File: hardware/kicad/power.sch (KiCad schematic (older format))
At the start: 12 parts, among them U2 ME6210, U3 ME6210, U4 TLV61046ADB

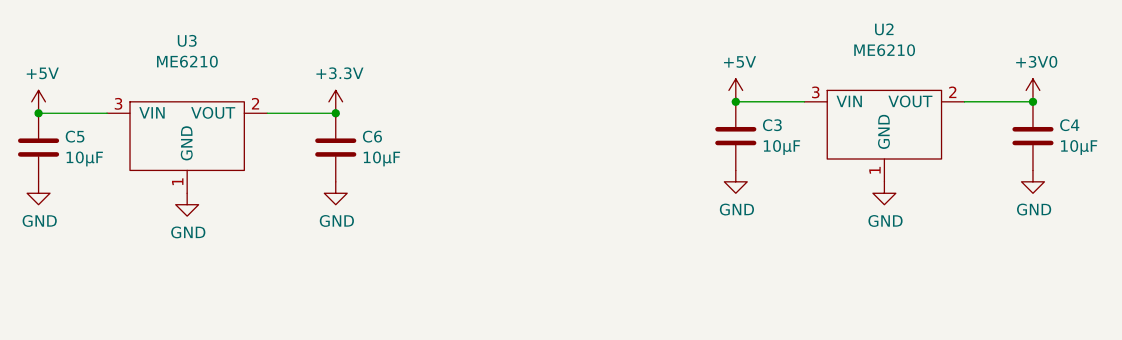
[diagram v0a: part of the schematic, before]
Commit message: Carify power IC symbol names
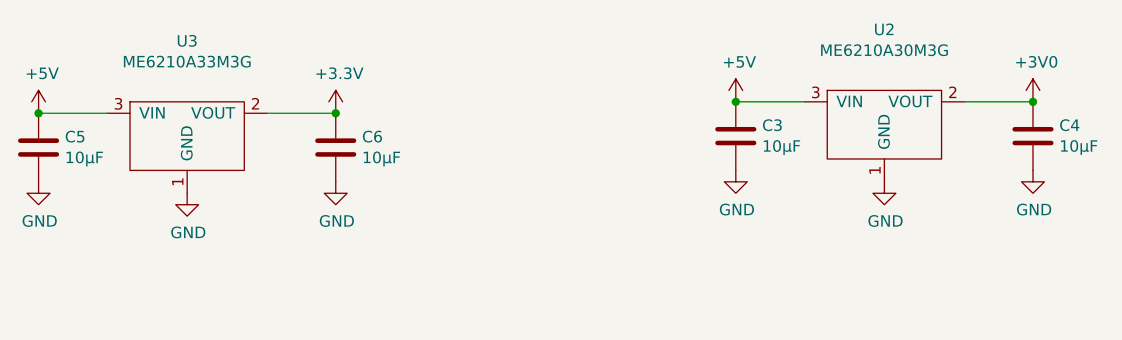
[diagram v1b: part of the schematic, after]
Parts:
- U2: value ME6210 -> ME6210A30M3G
- U3: value ME6210 -> ME6210A33M3G
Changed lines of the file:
@@
 P 4150 2150
 F 0 "U3" H 4150 2565 50  0000 C CNN
-F 1 "ME6210" H 4150 2474 50  0000 C CNN
+F 1 "ME6210A33M3G" H 4150 2474 50  0000 C CNN
 F 2 "Package_TO_SOT_SMD:SOT-23" H 4150 1400 50  0001 C CNN
 F 3 "" H 4150 2150 50  0001 C CNN
@@
 P 7200 2100
 F 0 "U2" H 7200 2515 50  0000 C CNN
-F 1 "ME6210" H 7200 2424 50  0000 C CNN
+F 1 "ME6210A30M3G" H 7200 2424 50  0000 C CNN
 F 2 "Package_TO_SOT_SMD:SOT-23" H 7200 1350 50  0001 C CNN
 F 3 "" H 7200 2100 50  0001 C CNN

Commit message: Add digikey bom alternative
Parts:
- C3, C4, C5, C6: DigiKey (none) -> 478-10766-1-ND
- C7: DigiKey (none) -> 1276-1182-1-ND
- C8: DigiKey (none) -> 1276-1045-1-ND
- L1: DigiKey (none) -> 535-11587-1-ND
- R1: DigiKey (none) -> 311-1.00MHRCT-ND
- R2: DigiKey (none) -> 311-71.5KHRCT-ND
- U2: DigiKey (none) -> AP2125N-3.0TRG1
- U3: DigiKey (none) -> AP2125N-3.3TRG1
- U4: DigiKey (none) -> TLV61046ADBVR
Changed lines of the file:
@@
 F 3 "" H 4150 2150 50  0001 C CNN
 F 4 "C236680" H 4150 2150 50  0001 C CNN "LCSC"
+F 5 "AP2125N-3.3TRG1" H 4150 2150 50  0001 C CNN "DigiKey"
 	1    4150 2150
 	1    0    0    -1
@@
 F 3 "" H 7200 2100 50  0001 C CNN
 F 4 "C116985" H 7200 2100 50  0001 C CNN "LCSC"
+F 5 "AP2125N-3.0TRG1" H 7200 2100 50  0001 C CNN "DigiKey"
 	1    7200 2100
 	1    0    0    -1
@@
 F 3 "~" H 3500 2200 50  0001 C CNN
 F 4 "C19702" H 3500 2200 50  0001 C CNN "LCSC"
+F 5 "478-10766-1-ND" H 3500 2200 50  0001 C CNN "DigiKey"
 	1    3500 2200
 	1    0    0    -1
@@
 F 3 "~" H 4800 2200 50  0001 C CNN
 F 4 "C19702" H 4800 2200 50  0001 C CNN "LCSC"
+F 5 "478-10766-1-ND" H 4800 2200 50  0001 C CNN "DigiKey"
 	1    4800 2200
 	1    0    0    -1
@@
 F 3 "~" H 6550 2150 50  0001 C CNN
 F 4 "C19702" H 6550 2150 50  0001 C CNN "LCSC"
+F 5 "478-10766-1-ND" H 6550 2150 50  0001 C CNN "DigiKey"
 	1    6550 2150
 	1    0    0    -1
@@
 F 3 "~" H 7850 2150 50  0001 C CNN
 F 4 "C19702" H 7850 2150 50  0001 C CNN "LCSC"
+F 5 "478-10766-1-ND" H 7850 2150 50  0001 C CNN "DigiKey"
 	1    7850 2150
 	1    0    0    -1
@@
 F 3 "http://www.ti.com/lit/ds/symlink/tlv61046a.pdf" H 5750 4450 50  0001 C CNN
 F 4 "C464815" H 5750 4350 50  0001 C CNN "LCSC"
+F 5 "TLV61046ADBVR" H 5750 4350 50  0001 C CNN "DigiKey"
 	1    5750 4350
 	1    0    0    -1
@@
 F 3 "~" H 4800 4300 50  0001 C CNN
 F 4 "C15849" H 4800 4300 50  0001 C CNN "LCSC"
+F 5 "1276-1182-1-ND" H 4800 4300 50  0001 C CNN "DigiKey"
 	1    4800 4300
 	1    0    0    -1
@@
 F 3 "~" H 6400 4800 50  0001 C CNN
 F 4 "C23103" H 6400 4800 50  0001 C CNN "LCSC"
+F 5 "311-71.5KHRCT-ND" H 6400 4800 50  0001 C CNN "DigiKey"
 	1    6400 4800
 	1    0    0    -1
@@
 F 3 "~" H 6800 4400 50  0001 C CNN
 F 4 "C19666" H 6800 4400 50  0001 C CNN "LCSC"
+F 5 "1276-1045-1-ND" H 6800 4400 50  0001 C CNN "DigiKey"
 	1    6800 4400
 	1    0    0    -1
@@
 F 3 "~" H 5750 3700 50  0001 C CNN
 F 4 "C1035" H 5750 3700 50  0001 C CNN "LCSC"
+F 5 "535-11587-1-ND" H 5750 3700 50  0001 C CNN "DigiKey"
 	1    5750 3700
 	0    -1   -1   0
@@
 F 3 "~" H 6400 4400 50  0001 C CNN
 F 4 "C22935" H 6400 4400 50  0001 C CNN "LCSC"
+F 5 "311-1.00MHRCT-ND" H 6400 4400 50  0001 C CNN "DigiKey"
 	1    6400 4400
 	1    0    0    -1

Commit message: Update BOM
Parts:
- C3, C4, C5, C6: Description (none) -> CAP CER 10UF 10V X5R 0603; DigiKey 478-10766-1-ND -> (none); Manufacturer (none) -> AVX Corporation; Mfg Part # (none) -> 0603ZD106KAT2A
- C7: Description (none) -> CAP CER 1UF 10V X5R 0603; DigiKey 1276-1182-1-ND -> (none); Manufacturer (none) -> Samsung Electro-Mechanics; Mfg Part # (none) -> CL10A105KP8NNNC
- C8: Description (none) -> CAP CER 4.7UF 6.3V X5R 0603; DigiKey 1276-1045-1-ND -> (none); Manufacturer (none) -> Samsung Electro-Mechanics; Mfg Part # (none) -> CL10A475KQ8NNNC
- L1: Description (none) -> FIXED IND 10UH 3MA 2.55 OHM SMD; DigiKey 535-11587-1-ND -> (none); Manufacturer (none) -> Abracon LLC; Mfg Part # (none) -> AIML-0603-100K-T
- R1: Description (none) -> RES SMD 1M OHM 1% 1/10W 0603; DigiKey 311-1.00MHRCT-ND -> (none); Manufacturer (none) -> Yageo; Mfg Part # (none) -> RC0603FR-071ML
- R2: Description (none) -> RES SMD 71.5K OHM 1% 1/10W 0603; DigiKey 311-71.5KHRCT-ND -> (none); Manufacturer (none) -> Yageo; Mfg Part # (none) -> RC0603FR-0771K5L
- U2: Description (none) -> IC REG LINEAR 3V 300MA SOT23-3; DigiKey AP2125N-3.0TRG1 -> (none); Manufacturer (none) -> Diodes Incorporated; Mfg Part # (none) -> AP2125N-3.0TRG1
- U3: Description (none) -> IC REG LINEAR 3.3V 300MA SOT23-3; DigiKey AP2125N-3.3TRG1 -> (none); Manufacturer (none) -> Diodes Incorporated; Mfg Part # (none) -> AP2125N-3.3TRG1
- U4: Description (none) -> IC REG BOOST ADJ SOT23-6; DigiKey TLV61046ADBVR -> (none); Manufacturer (none) -> Texas Instruments; Mfg Part # (none) -> TLV61046ADBVR
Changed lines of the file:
@@
 F 3 "" H 4150 2150 50  0001 C CNN
 F 4 "C236680" H 4150 2150 50  0001 C CNN "LCSC"
-F 5 "AP2125N-3.3TRG1" H 4150 2150 50  0001 C CNN "DigiKey"
+F 5 "" H 4150 2150 50  0001 C CNN "DigiKey"
+F 6 "AP2125N-3.3TRG1" H 4150 2150 50  0001 C CNN "Mfg Part #"
+F 7 "IC REG LINEAR 3.3V 300MA SOT23-3" H 4150 2150 50  0001 C CNN "Description"
+F 8 "Diodes Incorporated" H 4150 2150 50  0001 C CNN "Manufacturer"
 	1    4150 2150
 	1    0    0    -1
@@
 F 3 "" H 7200 2100 50  0001 C CNN
 F 4 "C116985" H 7200 2100 50  0001 C CNN "LCSC"
-F 5 "AP2125N-3.0TRG1" H 7200 2100 50  0001 C CNN "DigiKey"
+F 5 "" H 7200 2100 50  0001 C CNN "DigiKey"
+F 6 "AP2125N-3.0TRG1" H 7200 2100 50  0001 C CNN "Mfg Part #"
+F 7 "IC REG LINEAR 3V 300MA SOT23-3" H 7200 2100 50  0001 C CNN "Description"
+F 8 "Diodes Incorporated" H 7200 2100 50  0001 C CNN "Manufacturer"
 	1    7200 2100
 	1    0    0    -1
@@
 F 3 "~" H 3500 2200 50  0001 C CNN
 F 4 "C19702" H 3500 2200 50  0001 C CNN "LCSC"
-F 5 "478-10766-1-ND" H 3500 2200 50  0001 C CNN "DigiKey"
+F 5 "" H 3500 2200 50  0001 C CNN "DigiKey"
+F 6 "0603ZD106KAT2A" H 3500 2200 50  0001 C CNN "Mfg Part #"
+F 7 "CAP CER 10UF 10V X5R 0603" H 3500 2200 50  0001 C CNN "Description"
+F 8 "AVX Corporation" H 3500 2200 50  0001 C CNN "Manufacturer"
 	1    3500 2200
 	1    0    0    -1
@@
 F 3 "~" H 4800 2200 50  0001 C CNN
 F 4 "C19702" H 4800 2200 50  0001 C CNN "LCSC"
-F 5 "478-10766-1-ND" H 4800 2200 50  0001 C CNN "DigiKey"
+F 5 "" H 4800 2200 50  0001 C CNN "DigiKey"
+F 6 "0603ZD106KAT2A" H 4800 2200 50  0001 C CNN "Mfg Part #"
+F 7 "CAP CER 10UF 10V X5R 0603" H 4800 2200 50  0001 C CNN "Description"
+F 8 "AVX Corporation" H 4800 2200 50  0001 C CNN "Manufacturer"
 	1    4800 2200
 	1    0    0    -1
@@
 F 3 "~" H 6550 2150 50  0001 C CNN
 F 4 "C19702" H 6550 2150 50  0001 C CNN "LCSC"
-F 5 "478-10766-1-ND" H 6550 2150 50  0001 C CNN "DigiKey"
+F 5 "" H 6550 2150 50  0001 C CNN "DigiKey"
+F 6 "0603ZD106KAT2A" H 6550 2150 50  0001 C CNN "Mfg Part #"
+F 7 "CAP CER 10UF 10V X5R 0603" H 6550 2150 50  0001 C CNN "Description"
+F 8 "AVX Corporation" H 6550 2150 50  0001 C CNN "Manufacturer"
 	1    6550 2150
 	1    0    0    -1
@@
 F 3 "~" H 7850 2150 50  0001 C CNN
 F 4 "C19702" H 7850 2150 50  0001 C CNN "LCSC"
-F 5 "478-10766-1-ND" H 7850 2150 50  0001 C CNN "DigiKey"
+F 5 "" H 7850 2150 50  0001 C CNN "DigiKey"
+F 6 "0603ZD106KAT2A" H 7850 2150 50  0001 C CNN "Mfg Part #"
+F 7 "CAP CER 10UF 10V X5R 0603" H 7850 2150 50  0001 C CNN "Description"
+F 8 "AVX Corporation" H 7850 2150 50  0001 C CNN "Manufacturer"
 	1    7850 2150
 	1    0    0    -1
@@
 F 3 "http://www.ti.com/lit/ds/symlink/tlv61046a.pdf" H 5750 4450 50  0001 C CNN
 F 4 "C464815" H 5750 4350 50  0001 C CNN "LCSC"
-F 5 "TLV61046ADBVR" H 5750 4350 50  0001 C CNN "DigiKey"
+F 5 "" H 5750 4350 50  0001 C CNN "DigiKey"
+F 6 "TLV61046ADBVR" H 5750 4350 50  0001 C CNN "Mfg Part #"
+F 7 "IC REG BOOST ADJ SOT23-6" H 5750 4350 50  0001 C CNN "Description"
+F 8 "Texas Instruments" H 5750 4350 50  0001 C CNN "Manufacturer"
 	1    5750 4350
 	1    0    0    -1
@@
 F 3 "~" H 4800 4300 50  0001 C CNN
 F 4 "C15849" H 4800 4300 50  0001 C CNN "LCSC"
-F 5 "1276-1182-1-ND" H 4800 4300 50  0001 C CNN "DigiKey"
+F 5 "" H 4800 4300 50  0001 C CNN "DigiKey"
+F 6 "CL10A105KP8NNNC" H 4800 4300 50  0001 C CNN "Mfg Part #"
+F 7 "CAP CER 1UF 10V X5R 0603" H 4800 4300 50  0001 C CNN "Description"
+F 8 "Samsung Electro-Mechanics" H 4800 4300 50  0001 C CNN "Manufacturer"
 	1    4800 4300
 	1    0    0    -1
@@
 F 3 "~" H 6400 4800 50  0001 C CNN
 F 4 "C23103" H 6400 4800 50  0001 C CNN "LCSC"
-F 5 "311-71.5KHRCT-ND" H 6400 4800 50  0001 C CNN "DigiKey"
+F 5 "" H 6400 4800 50  0001 C CNN "DigiKey"
+F 6 "RC0603FR-0771K5L" H 6400 4800 50  0001 C CNN "Mfg Part #"
+F 7 "RES SMD 71.5K OHM 1% 1/10W 0603" H 6400 4800 50  0001 C CNN "Description"
+F 8 "Yageo" H 6400 4800 50  0001 C CNN "Manufacturer"
 	1    6400 4800
 	1    0    0    -1
@@
 F 3 "~" H 6800 4400 50  0001 C CNN
 F 4 "C19666" H 6800 4400 50  0001 C CNN "LCSC"
-F 5 "1276-1045-1-ND" H 6800 4400 50  0001 C CNN "DigiKey"
+F 5 "" H 6800 4400 50  0001 C CNN "DigiKey"
+F 6 "CL10A475KQ8NNNC" H 6800 4400 50  0001 C CNN "Mfg Part #"
+F 7 "CAP CER 4.7UF 6.3V X5R 0603" H 6800 4400 50  0001 C CNN "Description"
+F 8 "Samsung Electro-Mechanics" H 6800 4400 50  0001 C CNN "Manufacturer"
 	1    6800 4400
 	1    0    0    -1
@@
 F 3 "~" H 5750 3700 50  0001 C CNN
 F 4 "C1035" H 5750 3700 50  0001 C CNN "LCSC"
-F 5 "535-11587-1-ND" H 5750 3700 50  0001 C CNN "DigiKey"
+F 5 "" H 5750 3700 50  0001 C CNN "DigiKey"
+F 6 "AIML-0603-100K-T" H 5750 3700 50  0001 C CNN "Mfg Part #"
+F 7 "FIXED IND 10UH 3MA 2.55 OHM SMD" H 5750 3700 50  0001 C CNN "Description"
+F 8 "Abracon LLC" H 5750 3700 50  0001 C CNN "Manufacturer"
 	1    5750 3700
 	0    -1   -1   0
@@
 F 3 "~" H 6400 4400 50  0001 C CNN
 F 4 "C22935" H 6400 4400 50  0001 C CNN "LCSC"
-F 5 "311-1.00MHRCT-ND" H 6400 4400 50  0001 C CNN "DigiKey"
+F 5 "" H 6400 4400 50  0001 C CNN "DigiKey"
+F 6 "RC0603FR-071ML" H 6400 4400 50  0001 C CNN "Mfg Part #"
+F 7 "RES SMD 1M OHM 1% 1/10W 0603" H 6400 4400 50  0001 C CNN "Description"
+F 8 "Yageo" H 6400 4400 50  0001 C CNN "Manufacturer"
 	1    6400 4400
 	1    0    0    -1
